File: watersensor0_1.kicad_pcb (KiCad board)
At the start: 2 copper layers, 25.4 x 139.7 mm, 20 parts, among them U1 DIP-8_W7.62mm, U2 DIP-8_W7.62mm

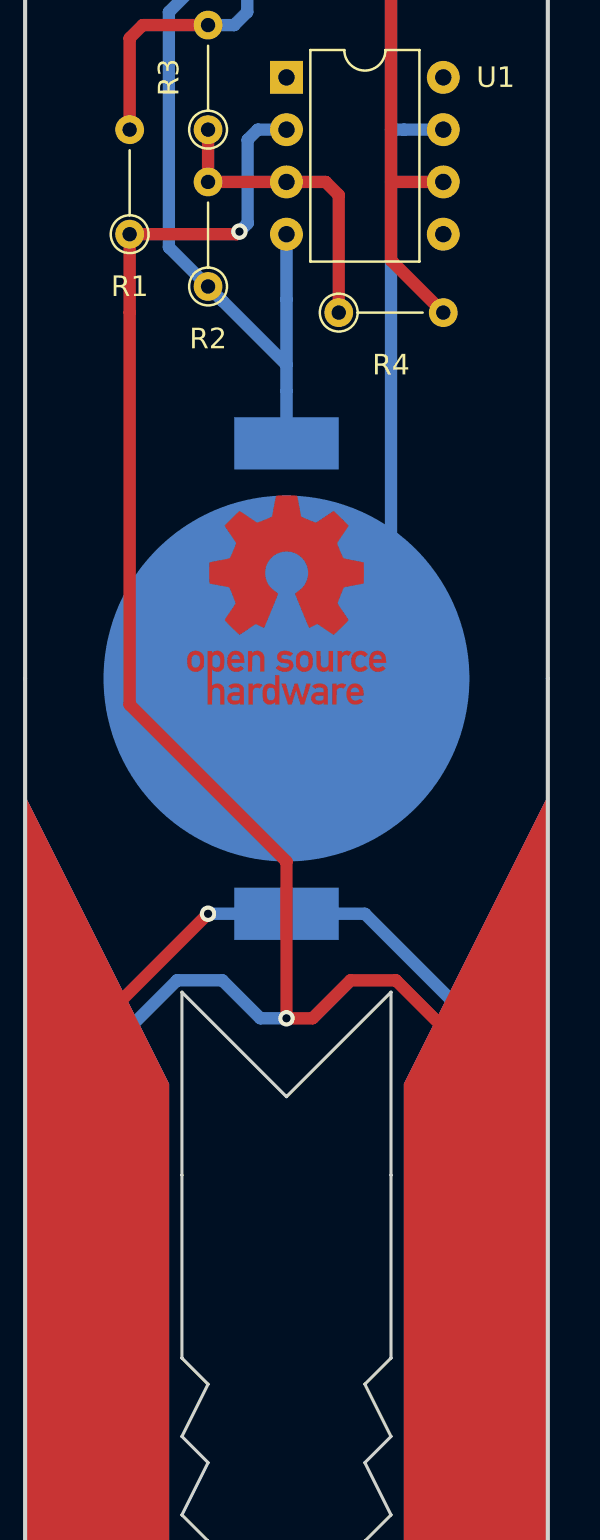
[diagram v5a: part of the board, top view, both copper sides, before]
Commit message: fixed battery polarity
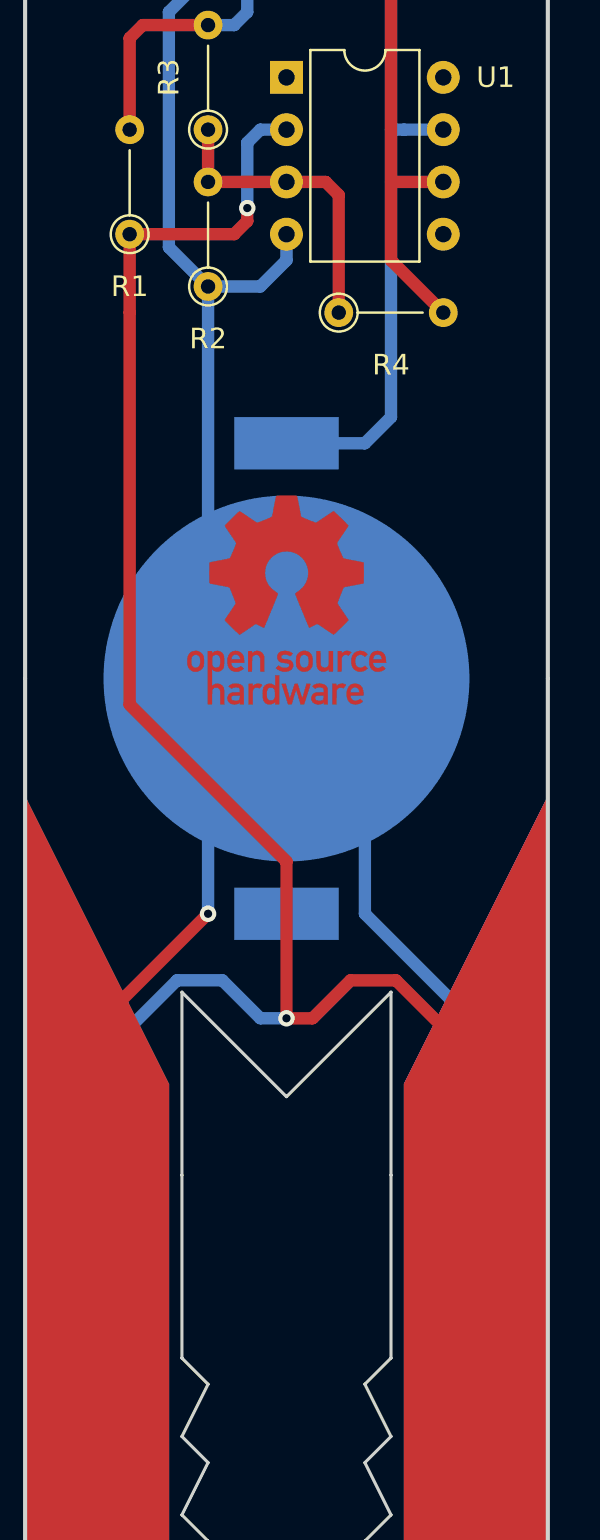
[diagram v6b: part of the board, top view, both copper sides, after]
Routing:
- net (no net): track 476.0 -> 468.7 mm
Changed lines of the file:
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@@
     (thickness 1.6)
     (drawings 46)
-    (tracks 100)
+    (tracks 103)
     (zones 0)
     (modules 20)
@@
     (solder_mask_min_width 0.25)
     (aux_axis_origin 0 0)
-    (visible_elements 7FFFFFFF)
+    (visible_elements FFFFFF7F)
     (pcbplotparams
       (layerselection 0x010fc_ffffffff)
@@
   (segment (start 120.015 60.325) (end 123.19 60.325) (width 0.6) (layer F.Cu) (net 0))
   (segment (start 134.62 37.465) (end 134.62 41.275) (width 0.6) (layer F.Cu) (net 0))
-  (segment (start 127 84.455) (end 127 83.185) (width 0.6) (layer B.Cu) (net 0))
   (segment (start 132.715 70.485) (end 134.62 70.485) (width 0.6) (layer B.Cu) (net 0))
   (segment (start 132.08 92.075) (end 127 97.155) (width 0.6) (layer B.Cu) (net 0))
   (segment (start 132.715 70.485) (end 132.08 70.485) (width 0.6) (layer B.Cu) (net 0))
-  (segment (start 132.08 70.485) (end 132.08 92.075) (width 0.6) (layer B.Cu) (net 0))
   (segment (start 129.54 37.465) (end 128.27 36.195) (width 0.6) (layer F.Cu) (net 0))
   (segment (start 128.27 36.195) (end 128.27 33.02) (width 0.6) (layer F.Cu) (net 0))
@@
   (segment (start 123.19 38.735) (end 125.73 36.195) (width 0.6) (layer F.Cu) (net 0))
   (segment (start 116.84 132.715) (end 116.84 111.125) (width 0.6) (layer B.Cu) (net 0))
-  (via (at 127 113.665) (size 0.8) (drill 0.4) (layers F.Cu B.Cu) (net 0) (status 1000000))
+  (via (at 127 113.665) (size 0.8) (drill 0.4) (layers F.Cu B.Cu) (net 0))
   (segment (start 127 113.665) (end 128.27 113.665) (width 0.6) (layer F.Cu) (net 0))
   (segment (start 132.318176 111.81999) (end 137.16 116.661814) (width 0.6) (layer F.Cu) (net 0))
@@
   (segment (start 123.19 50.165) (end 125.095 52.07) (width 0.6) (layer B.Cu) (net 0))
   (segment (start 132.08 63.5) (end 132.08 70.485) (width 0.6) (layer B.Cu) (net 0))
-  (segment (start 127 78.74) (end 127 75.565) (width 0.6) (layer B.Cu) (net 0))
-  (segment (start 123.19 78.105) (end 123.889999 78.804999) (width 0.6) (layer B.Cu) (net 0))
-  (segment (start 127 83.185) (end 127 81.915) (width 0.6) (layer B.Cu) (net 0))
-  (segment (start 123.889999 78.804999) (end 127 81.915) (width 0.6) (layer B.Cu) (net 0))
-  (segment (start 127 81.915) (end 127 78.74) (width 0.6) (layer B.Cu) (net 0))
   (segment (start 125.095 62.865) (end 132.08 62.865) (width 0.6) (layer B.Cu) (net 0))
   (segment (start 132.08 61.595) (end 132.08 62.865) (width 0.6) (layer B.Cu) (net 0))
@@
   (segment (start 129.54 48.895) (end 129.54 57.15) (width 0.6) (layer F.Cu) (net 0))
   (segment (start 129.54 57.15) (end 128.905 57.785) (width 0.6) (layer F.Cu) (net 0))
-  (segment (start 137.16 114.935) (end 137.16 132.715) (width 0.6) (layer B.Cu) (net 0))
-  (segment (start 130.81 108.585) (end 137.16 114.935) (width 0.6) (layer B.Cu) (net 0))
   (segment (start 123.19 108.585) (end 116.84 114.935) (width 0.6) (layer F.Cu) (net 0))
   (segment (start 116.84 114.935) (end 116.84 132.715) (width 0.6) (layer F.Cu) (net 0))
-  (segment (start 137.16 132.715) (end 137.16 111.125) (width 0.6) (layer B.Cu) (net 0))
   (via (at 123.19 108.585) (size 0.8) (drill 0.4) (layers F.Cu B.Cu) (net 0))
-  (segment (start 130.81 108.585) (end 123.19 108.585) (width 0.6) (layer B.Cu) (net 0))
   (segment (start 127 55.245) (end 128.905 55.245) (width 0.6) (layer B.Cu) (net 0))
   (segment (start 128.905 55.245) (end 129.54 54.61) (width 0.6) (layer B.Cu) (net 0))
@@
   (segment (start 119.38 46.99) (end 119.38 55.325) (width 0.6) (layer B.Cu) (net 0))
   (segment (start 126.365 46.355) (end 120.015 46.355) (width 0.6) (layer B.Cu) (net 0))
-  (via (at 124.714 75.438) (size 0.8) (drill 0.4) (layers F.Cu B.Cu) (net 0))
-  (segment (start 119.38 75.565) (end 124.587 75.565) (width 0.6) (layer F.Cu) (net 0))
-  (segment (start 124.587 75.565) (end 124.714 75.438) (width 0.6) (layer F.Cu) (net 0))
-  (segment (start 125.113999 75.038001) (end 125.113999 70.974001) (width 0.6) (layer B.Cu) (net 0))
-  (segment (start 124.714 75.438) (end 125.113999 75.038001) (width 0.6) (layer B.Cu) (net 0))
-  (segment (start 125.603 70.485) (end 127 70.485) (width 0.6) (layer B.Cu) (net 0))
-  (segment (start 125.113999 70.974001) (end 125.603 70.485) (width 0.6) (layer B.Cu) (net 0))
+  (segment (start 127 70.485) (end 125.73 70.485) (width 0.6) (layer B.Cu) (net 0))
+  (segment (start 125.73 70.485) (end 125.095 71.12) (width 0.6) (layer B.Cu) (net 0))
+  (segment (start 125.095 71.12) (end 125.095 74.295) (width 0.6) (layer B.Cu) (net 0))
+  (via (at 125.095 74.295) (size 0.8) (drill 0.4) (layers F.Cu B.Cu) (net 0))
+  (segment (start 125.095 74.295) (end 125.095 74.93) (width 0.6) (layer F.Cu) (net 0))
+  (segment (start 124.46 75.565) (end 119.38 75.565) (width 0.6) (layer F.Cu) (net 0))
+  (segment (start 125.095 74.93) (end 124.46 75.565) (width 0.6) (layer F.Cu) (net 0))
+  (segment (start 127 75.565) (end 127 76.835) (width 0.6) (layer B.Cu) (net 0))
+  (segment (start 125.73 78.105) (end 123.19 78.105) (width 0.6) (layer B.Cu) (net 0))
+  (segment (start 127 76.835) (end 125.73 78.105) (width 0.6) (layer B.Cu) (net 0))
+  (segment (start 123.19 93.345) (end 127 97.155) (width 0.6) (layer B.Cu) (net 0))
+  (segment (start 123.19 78.105) (end 123.19 93.345) (width 0.6) (layer B.Cu) (net 0))
+  (segment (start 132.08 70.485) (end 132.08 84.455) (width 0.6) (layer B.Cu) (net 0))
+  (segment (start 132.08 84.455) (end 130.81 85.725) (width 0.6) (layer B.Cu) (net 0))
+  (segment (start 123.19 100.965) (end 127 97.155) (width 0.6) (layer B.Cu) (net 0))
+  (segment (start 123.19 108.585) (end 123.19 100.965) (width 0.6) (layer B.Cu) (net 0))
+  (segment (start 137.16 111.125) (end 137.16 114.935) (width 0.6) (layer B.Cu) (net 0))
+  (segment (start 130.81 100.965) (end 127 97.155) (width 0.6) (layer B.Cu) (net 0))
+  (segment (start 130.81 108.585) (end 130.81 100.965) (width 0.6) (layer B.Cu) (net 0))
+  (segment (start 137.16 114.935) (end 130.81 108.585) (width 0.6) (layer B.Cu) (net 0))
+  (segment (start 130.81 85.725) (end 127 85.725) (width 0.6) (layer B.Cu) (net 0))
 )

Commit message: removed unneeded via
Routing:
- net (no net): track 468.7 -> 467.9 mm, vias 3 -> 2
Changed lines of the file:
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@@
     (thickness 1.6)
     (drawings 46)
-    (tracks 103)
+    (tracks 100)
     (zones 0)
     (modules 20)
@@
     (uvia_dia 0.3)
     (uvia_drill 0.1)
+  )
+  (module Package_DIP:DIP-8_W7.62mm (layer F.Cu)
+    (at 127 67.945)
+    (descr "8-lead though-hole mounted DIP package, row spacing 7.62 mm (300 mils)")
+    (tags "THT DIP DIL PDIP 2.54mm 7.62mm 300mil")
+    (fp_text reference U1 (at 10.16 0) (layer F.SilkS)
+      (effects (font (size 1 1) (thickness 0.15)))
+    )
+    (fp_text value DIP-8_W7.62mm (at 3.81 9.95) (layer F.Fab)
+      (effects (font (size 1 1) (thickness 0.15)))
+    )
+    (fp_text user %R (at 3.81 3.81) (layer F.Fab)
+      (effects (font (size 1 1) (thickness 0.15)))
+    )
+    (fp_line (start 8.7 -1.55) (end -1.1 -1.55) (layer F.CrtYd) (width 0.05))
+    (fp_line (start 8.7 9.15) (end 8.7 -1.55) (layer F.CrtYd) (width 0.05))
+    (fp_line (start -1.1 9.15) (end 8.7 9.15) (layer F.CrtYd) (width 0.05))
+    (fp_line (start -1.1 -1.55) (end -1.1 9.15) (layer F.CrtYd) (width 0.05))
+    (fp_line (start 6.46 -1.33) (end 4.81 -1.33) (layer F.SilkS) (width 0.12))
+    (fp_line (start 6.46 8.95) (end 6.46 -1.33) (layer F.SilkS) (width 0.12))
+    (fp_line (start 1.16 8.95) (end 6.46 8.95) (layer F.SilkS) (width 0.12))
+    (fp_line (start 1.16 -1.33) (end 1.16 8.95) (layer F.SilkS) (width 0.12))
+    (fp_line (start 2.81 -1.33) (end 1.16 -1.33) (layer F.SilkS) (width 0.12))
+    (fp_line (start 0.635 -0.27) (end 1.635 -1.27) (layer F.Fab) (width 0.1))
+    (fp_line (start 0.635 8.89) (end 0.635 -0.27) (layer F.Fab) (width 0.1))
+    (fp_line (start 6.985 8.89) (end 0.635 8.89) (layer F.Fab) (width 0.1))
+    (fp_line (start 6.985 -1.27) (end 6.985 8.89) (layer F.Fab) (width 0.1))
+    (fp_line (start 1.635 -1.27) (end 6.985 -1.27) (layer F.Fab) (width 0.1))
+    (fp_arc (start 3.81 -1.33) (end 2.81 -1.33) (angle -180) (layer F.SilkS) (width 0.12))
+    (pad 8 thru_hole oval (at 7.62 0) (size 1.6 1.6) (drill 0.8) (layers *.Cu *.Mask))
+    (pad 4 thru_hole oval (at 0 7.62) (size 1.6 1.6) (drill 0.8) (layers *.Cu *.Mask))
+    (pad 7 thru_hole oval (at 7.62 2.54) (size 1.6 1.6) (drill 0.8) (layers *.Cu *.Mask))
+    (pad 3 thru_hole oval (at 0 5.08) (size 1.6 1.6) (drill 0.8) (layers *.Cu *.Mask))
+    (pad 6 thru_hole oval (at 7.62 5.08) (size 1.6 1.6) (drill 0.8) (layers *.Cu *.Mask))
+    (pad 2 thru_hole oval (at 0 2.54) (size 1.6 1.6) (drill 0.8) (layers *.Cu *.Mask))
+    (pad 5 thru_hole oval (at 7.62 7.62) (size 1.6 1.6) (drill 0.8) (layers *.Cu *.Mask))
+    (pad 1 thru_hole rect (at 0 0) (size 1.6 1.6) (drill 0.8) (layers *.Cu *.Mask))
+    (model ${KISYS3DMOD}/Package_DIP.3dshapes/DIP-8_W7.62mm.wrl
+      (at (xyz 0 0 0))
+      (scale (xyz 1 1 1))
+      (rotate (xyz 0 0 0))
+    )
   )
   (module WaterSensorProngs (layer B.Cu)
@@
     )
   )
-  (module Package_DIP:DIP-8_W7.62mm (layer F.Cu)
-    (at 127 67.945)
-    (descr "8-lead though-hole mounted DIP package, row spacing 7.62 mm (300 mils)")
-    (tags "THT DIP DIL PDIP 2.54mm 7.62mm 300mil")
-    (fp_text reference U1 (at 10.16 0) (layer F.SilkS)
-      (effects (font (size 1 1) (thickness 0.15)))
-    )
-    (fp_text value DIP-8_W7.62mm (at 3.81 9.95) (layer F.Fab)
-      (effects (font (size 1 1) (thickness 0.15)))
-    )
-    (fp_text user %R (at 3.81 3.81) (layer F.Fab)
-      (effects (font (size 1 1) (thickness 0.15)))
-    )
-    (fp_line (start 8.7 -1.55) (end -1.1 -1.55) (layer F.CrtYd) (width 0.05))
-    (fp_line (start 8.7 9.15) (end 8.7 -1.55) (layer F.CrtYd) (width 0.05))
-    (fp_line (start -1.1 9.15) (end 8.7 9.15) (layer F.CrtYd) (width 0.05))
-    (fp_line (start -1.1 -1.55) (end -1.1 9.15) (layer F.CrtYd) (width 0.05))
-    (fp_line (start 6.46 -1.33) (end 4.81 -1.33) (layer F.SilkS) (width 0.12))
-    (fp_line (start 6.46 8.95) (end 6.46 -1.33) (layer F.SilkS) (width 0.12))
-    (fp_line (start 1.16 8.95) (end 6.46 8.95) (layer F.SilkS) (width 0.12))
-    (fp_line (start 1.16 -1.33) (end 1.16 8.95) (layer F.SilkS) (width 0.12))
-    (fp_line (start 2.81 -1.33) (end 1.16 -1.33) (layer F.SilkS) (width 0.12))
-    (fp_line (start 0.635 -0.27) (end 1.635 -1.27) (layer F.Fab) (width 0.1))
-    (fp_line (start 0.635 8.89) (end 0.635 -0.27) (layer F.Fab) (width 0.1))
-    (fp_line (start 6.985 8.89) (end 0.635 8.89) (layer F.Fab) (width 0.1))
-    (fp_line (start 6.985 -1.27) (end 6.985 8.89) (layer F.Fab) (width 0.1))
-    (fp_line (start 1.635 -1.27) (end 6.985 -1.27) (layer F.Fab) (width 0.1))
-    (fp_arc (start 3.81 -1.33) (end 2.81 -1.33) (angle -180) (layer F.SilkS) (width 0.12))
-    (pad 8 thru_hole oval (at 7.62 0) (size 1.6 1.6) (drill 0.8) (layers *.Cu *.Mask))
-    (pad 4 thru_hole oval (at 0 7.62) (size 1.6 1.6) (drill 0.8) (layers *.Cu *.Mask))
-    (pad 7 thru_hole oval (at 7.62 2.54) (size 1.6 1.6) (drill 0.8) (layers *.Cu *.Mask))
-    (pad 3 thru_hole oval (at 0 5.08) (size 1.6 1.6) (drill 0.8) (layers *.Cu *.Mask))
-    (pad 6 thru_hole oval (at 7.62 5.08) (size 1.6 1.6) (drill 0.8) (layers *.Cu *.Mask))
-    (pad 2 thru_hole oval (at 0 2.54) (size 1.6 1.6) (drill 0.8) (layers *.Cu *.Mask))
-    (pad 5 thru_hole oval (at 7.62 7.62) (size 1.6 1.6) (drill 0.8) (layers *.Cu *.Mask))
-    (pad 1 thru_hole rect (at 0 0) (size 1.6 1.6) (drill 0.8) (layers *.Cu *.Mask))
-    (model ${KISYS3DMOD}/Package_DIP.3dshapes/DIP-8_W7.62mm.wrl
-      (at (xyz 0 0 0))
-      (scale (xyz 1 1 1))
-      (rotate (xyz 0 0 0))
-    )
-  )
   (module Resistor_THT:R_Axial_DIN0204_L3.6mm_D1.6mm_P5.08mm_Vertical (layer F.Cu)
     (at 129.54 79.375)
@@
   (segment (start 119.38 79.375) (end 119.38 98.425) (width 0.6) (layer F.Cu) (net 0))
   (segment (start 119.38 98.425) (end 127 106.045) (width 0.6) (layer F.Cu) (net 0))
-  (segment (start 123.19 70.485) (end 123.19 73.025) (width 0.6) (layer F.Cu) (net 0))
-  (segment (start 123.19 73.025) (end 127 73.025) (width 0.6) (layer F.Cu) (net 0))
-  (segment (start 129.54 79.375) (end 129.54 73.66) (width 0.6) (layer F.Cu) (net 0))
-  (segment (start 128.905 73.025) (end 127 73.025) (width 0.6) (layer F.Cu) (net 0))
-  (segment (start 129.54 73.66) (end 128.905 73.025) (width 0.6) (layer F.Cu) (net 0))
   (segment (start 132.08 76.835) (end 132.08 60.96) (width 0.6) (layer F.Cu) (net 0))
   (segment (start 123.19 47.625) (end 123.19 50.165) (width 0.6) (layer F.Cu) (net 0))
@@
   (segment (start 119.38 46.99) (end 119.38 55.325) (width 0.6) (layer B.Cu) (net 0))
   (segment (start 126.365 46.355) (end 120.015 46.355) (width 0.6) (layer B.Cu) (net 0))
-  (segment (start 127 70.485) (end 125.73 70.485) (width 0.6) (layer B.Cu) (net 0))
-  (segment (start 125.73 70.485) (end 125.095 71.12) (width 0.6) (layer B.Cu) (net 0))
-  (segment (start 125.095 71.12) (end 125.095 74.295) (width 0.6) (layer B.Cu) (net 0))
-  (via (at 125.095 74.295) (size 0.8) (drill 0.4) (layers F.Cu B.Cu) (net 0))
-  (segment (start 125.095 74.295) (end 125.095 74.93) (width 0.6) (layer F.Cu) (net 0))
-  (segment (start 124.46 75.565) (end 119.38 75.565) (width 0.6) (layer F.Cu) (net 0))
-  (segment (start 125.095 74.93) (end 124.46 75.565) (width 0.6) (layer F.Cu) (net 0))
-  (segment (start 127 75.565) (end 127 76.835) (width 0.6) (layer B.Cu) (net 0))
-  (segment (start 125.73 78.105) (end 123.19 78.105) (width 0.6) (layer B.Cu) (net 0))
-  (segment (start 127 76.835) (end 125.73 78.105) (width 0.6) (layer B.Cu) (net 0))
   (segment (start 123.19 93.345) (end 127 97.155) (width 0.6) (layer B.Cu) (net 0))
   (segment (start 123.19 78.105) (end 123.19 93.345) (width 0.6) (layer B.Cu) (net 0))
@@
   (segment (start 137.16 114.935) (end 130.81 108.585) (width 0.6) (layer B.Cu) (net 0))
   (segment (start 130.81 85.725) (end 127 85.725) (width 0.6) (layer B.Cu) (net 0))
+  (segment (start 124.46 78.105) (end 127 75.565) (width 0.6) (layer B.Cu) (net 0))
+  (segment (start 123.19 78.105) (end 124.46 78.105) (width 0.6) (layer B.Cu) (net 0))
+  (segment (start 125.095 74.93) (end 124.46 75.565) (width 0.6) (layer F.Cu) (net 0))
+  (segment (start 125.095 71.12) (end 125.095 74.93) (width 0.6) (layer F.Cu) (net 0))
+  (segment (start 124.46 75.565) (end 119.38 75.565) (width 0.6) (layer F.Cu) (net 0))
+  (segment (start 127 70.485) (end 125.73 70.485) (width 0.6) (layer F.Cu) (net 0))
+  (segment (start 125.73 70.485) (end 125.095 71.12) (width 0.6) (layer F.Cu) (net 0))
+  (segment (start 123.19 73.025) (end 127 73.025) (width 0.6) (layer B.Cu) (net 0))
+  (segment (start 127 73.025) (end 128.905 73.025) (width 0.6) (layer B.Cu) (net 0))
+  (segment (start 128.905 73.025) (end 129.54 73.66) (width 0.6) (layer B.Cu) (net 0))
+  (segment (start 129.54 73.66) (end 129.54 79.375) (width 0.6) (layer B.Cu) (net 0))
+  (segment (start 123.19 70.485) (end 123.19 73.025) (width 0.6) (layer B.Cu) (net 0))
 )

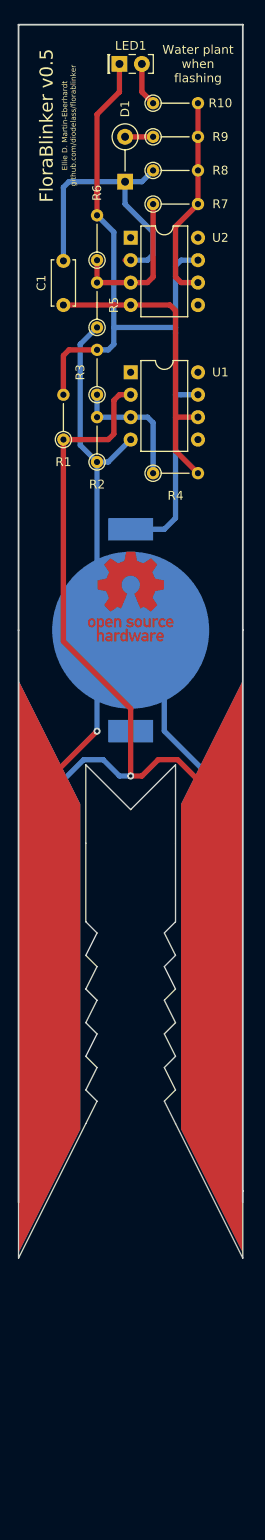
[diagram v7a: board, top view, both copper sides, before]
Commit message: reorganized wiring layout
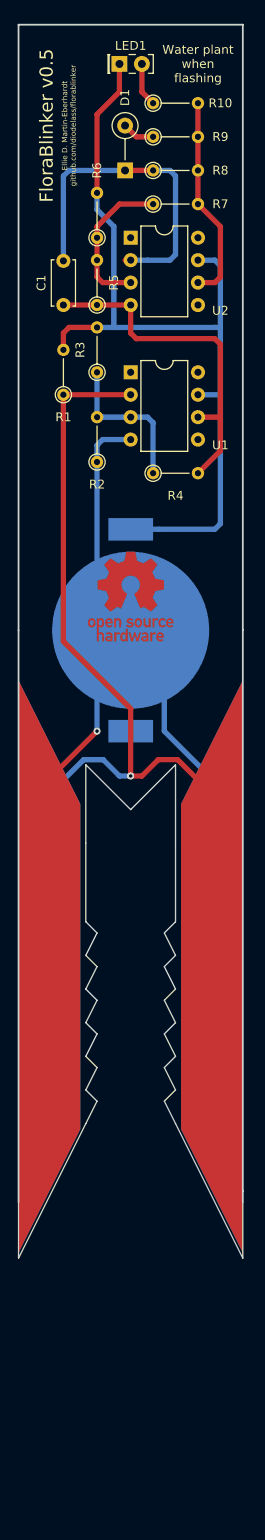
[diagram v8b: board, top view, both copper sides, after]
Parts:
- moved R1 5.08 mm to (119.4, 70.5)
- moved R3 2.54 mm to (123.2, 67.9)
- moved R5 2.54 mm to (123.2, 60.3)
- moved R6 2.54 mm to (123.2, 52.7)
- moved D1 1.27 mm to (126.4, 45.1)
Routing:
- net (no net): track 467.9 -> 472.4 mm
